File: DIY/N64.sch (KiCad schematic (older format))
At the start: 5 parts, among them P1 N64 Ctrl slot, P2 N64 Ctrl slot, P3 N64 Ctrl slot, P4 N64 Ctrl slot

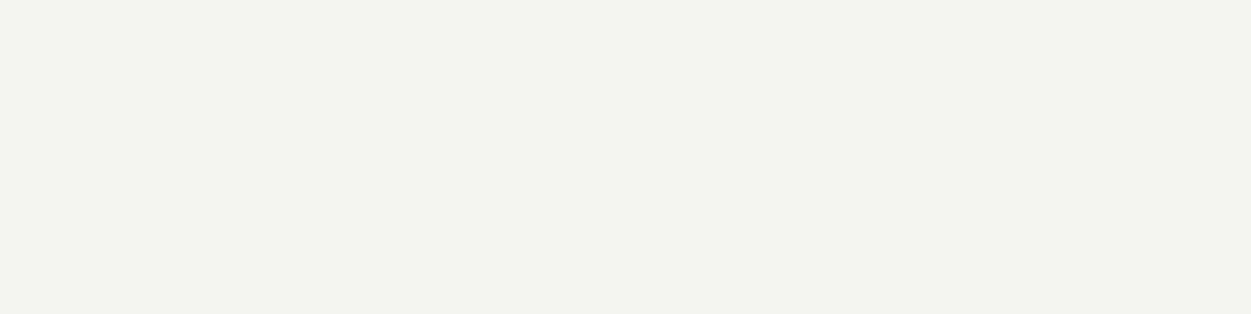
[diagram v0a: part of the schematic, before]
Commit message: [DIY] Add note to cable schematics to underline how important I39 is.
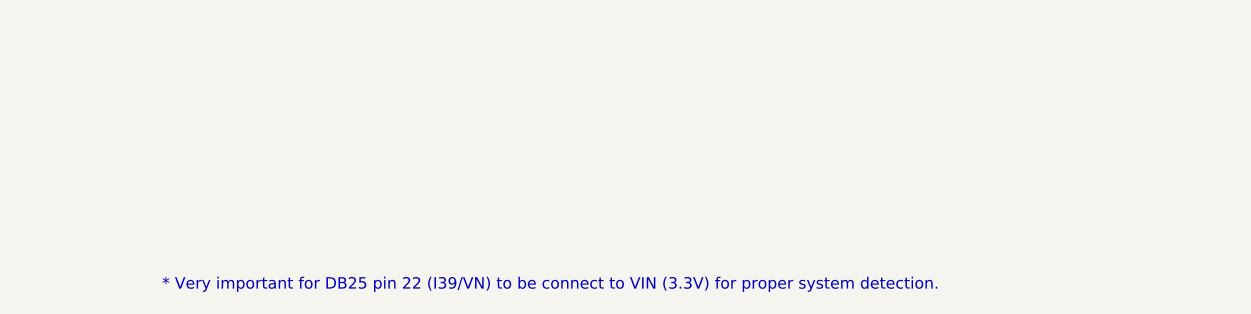
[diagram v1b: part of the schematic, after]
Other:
- note added: "* Very important for DB25 pin 22 (I39/VN) to be connect to VIN (3.3V) for proper system detection."
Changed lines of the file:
@@
 	6100 4650 6100 4550
 Connection ~ 6100 4550
+Text Notes 6350 6900 0    50   ~ 0
+* Very important for DB25 pin 22 (I39/VN) to be connect to VIN (3.3V) for proper system detection.
 $EndSCHEMATC

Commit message: Use new port symbol in cable schematic
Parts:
- P1, P2, P3, P4: symbol Connector_Generic:Conn_01x03 -> Connector_Gaming:N64
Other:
- note added: "Connectors facing console"
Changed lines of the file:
@@
 Sheet 5 7
 Title "BlueRetro - N64 adapter cable"
-Date "2020-08-22"
-Rev "v1.1"
-Comp ""
+Date "2020-10-02"
+Rev "v1.2"
+Comp "©2020 Jacques Gagnon, licensed under CC-BY-4.0"
 Comment1 ""
 Comment2 ""
@@
 $EndDescr
 $Comp
-L Connector_Generic:Conn_01x03 P?
+L Connector_Gaming:N64 P?
 U 1 1 5F47F7C8
-P 4650 2600
+P 4550 2500
 AR Path="/5F47F7C8" Ref="P?"  Part="1"
 AR Path="/5F457716/5F47F7C8" Ref="P1"  Part="1"
-F 0 "P1" H 4568 2917 50  0000 C CNN
-F 1 "N64 Ctrl slot" H 4568 2826 50  0000 C CNN
-F 2 "" H 4650 2600 50  0001 C CNN
-F 3 "~" H 4650 2600 50  0001 C CNN
-	1    4650 2600
-	-1   0    0    -1
-$EndComp
-$Comp
-L Connector_Generic:Conn_01x03 P?
+F 0 "P1" H 4550 2250 50  0000 C CNN
+F 1 "N64 Ctrl slot" H 4550 2350 50  0000 C CNN
+F 2 "" H 4550 2500 50  0001 C CNN
+F 3 "~" H 4550 2500 50  0001 C CNN
+	1    4550 2500
+	-1   0    0    1
+$EndComp
+$Comp
+L Connector_Gaming:N64 P?
 U 1 1 5F47F7CE
-P 4650 3250
+P 4550 3150
 AR Path="/5F47F7CE" Ref="P?"  Part="1"
 AR Path="/5F457716/5F47F7CE" Ref="P2"  Part="1"
-F 0 "P2" H 4568 3567 50  0000 C CNN
-F 1 "N64 Ctrl slot" H 4568 3476 50  0000 C CNN
-F 2 "" H 4650 3250 50  0001 C CNN
-F 3 "~" H 4650 3250 50  0001 C CNN
-	1    4650 3250
-	-1   0    0    -1
-$EndComp
-$Comp
-L Connector_Generic:Conn_01x03 P?
+F 0 "P2" H 4550 2900 50  0000 C CNN
+F 1 "N64 Ctrl slot" H 4550 3000 50  0000 C CNN
+F 2 "" H 4550 3150 50  0001 C CNN
+F 3 "~" H 4550 3150 50  0001 C CNN
+	1    4550 3150
+	-1   0    0    1
+$EndComp
+$Comp
+L Connector_Gaming:N64 P?
 U 1 1 5F47F7D4
-P 4650 3900
+P 4550 3800
 AR Path="/5F47F7D4" Ref="P?"  Part="1"
 AR Path="/5F457716/5F47F7D4" Ref="P3"  Part="1"
-F 0 "P3" H 4568 4217 50  0000 C CNN
-F 1 "N64 Ctrl slot" H 4568 4126 50  0000 C CNN
-F 2 "" H 4650 3900 50  0001 C CNN
-F 3 "~" H 4650 3900 50  0001 C CNN
-	1    4650 3900
-	-1   0    0    -1
-$EndComp
-$Comp
-L Connector_Generic:Conn_01x03 P?
+F 0 "P3" H 4550 3550 50  0000 C CNN
+F 1 "N64 Ctrl slot" H 4550 3650 50  0000 C CNN
+F 2 "" H 4550 3800 50  0001 C CNN
+F 3 "~" H 4550 3800 50  0001 C CNN
+	1    4550 3800
+	-1   0    0    1
+$EndComp
+$Comp
+L Connector_Gaming:N64 P?
 U 1 1 5F47F7DA
-P 4650 4550
+P 4550 4450
 AR Path="/5F47F7DA" Ref="P?"  Part="1"
 AR Path="/5F457716/5F47F7DA" Ref="P4"  Part="1"
-F 0 "P4" H 4568 4867 50  0000 C CNN
-F 1 "N64 Ctrl slot" H 4568 4776 50  0000 C CNN
-F 2 "" H 4650 4550 50  0001 C CNN
-F 3 "~" H 4650 4550 50  0001 C CNN
-	1    4650 4550
-	-1   0    0    -1
+F 0 "P4" H 4550 4200 50  0000 C CNN
+F 1 "N64 Ctrl slot" H 4550 4300 50  0000 C CNN
+F 2 "" H 4550 4450 50  0001 C CNN
+F 3 "~" H 4550 4450 50  0001 C CNN
+	1    4550 4450
+	-1   0    0    1
 $EndComp
 $Comp
@@
 Text Notes 6350 6900 0    50   ~ 0
 * Very important for DB25 pin 22 (I39/VN) to be connect to VIN (3.3V) for proper system detection.
+Text Notes 3250 3500 0    50   ~ 0
+Connectors facing console
 $EndSCHEMATC

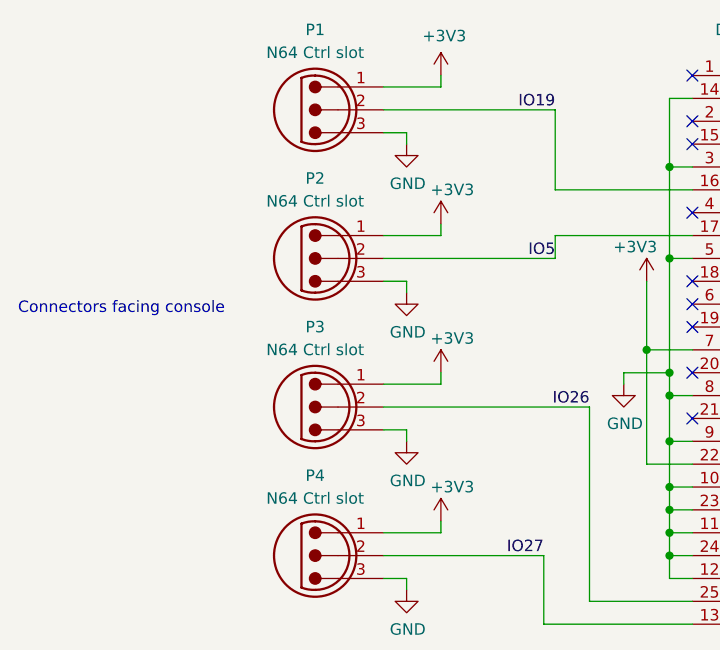
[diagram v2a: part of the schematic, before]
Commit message: Update adapter cable schematics
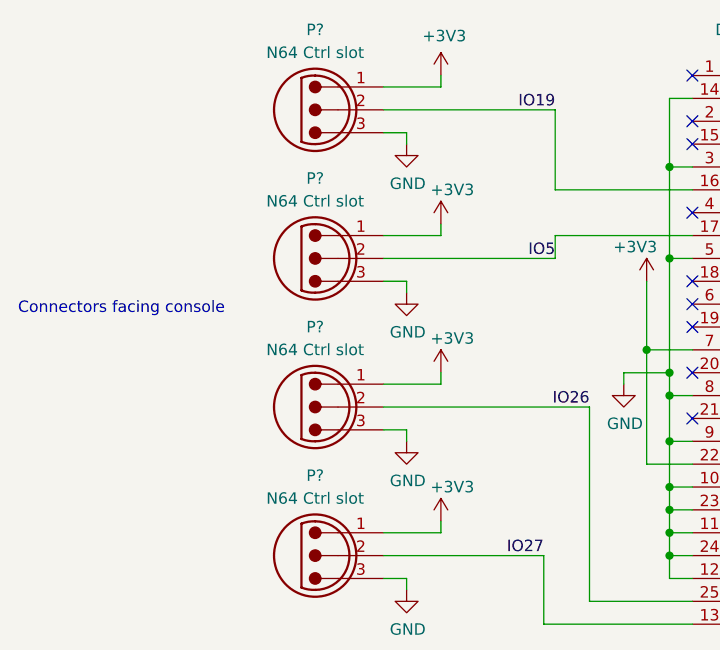
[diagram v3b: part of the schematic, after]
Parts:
- gave numbers to parts that had none: 1
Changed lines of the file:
@@
 $Descr USLetter 11000 8500
 encoding utf-8
-Sheet 5 7
+Sheet 5 10
 Title "BlueRetro - N64 adapter cable"
 Date "2020-10-02"
@@
 AR Path="/5F47F7C8" Ref="P?"  Part="1"
 AR Path="/5F457716/5F47F7C8" Ref="P1"  Part="1"
-F 0 "P1" H 4550 2250 50  0000 C CNN
+F 0 "P?" H 4550 2250 50  0000 C CNN
 F 1 "N64 Ctrl slot" H 4550 2350 50  0000 C CNN
 F 2 "" H 4550 2500 50  0001 C CNN
@@
 AR Path="/5F47F7CE" Ref="P?"  Part="1"
 AR Path="/5F457716/5F47F7CE" Ref="P2"  Part="1"
-F 0 "P2" H 4550 2900 50  0000 C CNN
+F 0 "P?" H 4550 2900 50  0000 C CNN
 F 1 "N64 Ctrl slot" H 4550 3000 50  0000 C CNN
 F 2 "" H 4550 3150 50  0001 C CNN
@@
 AR Path="/5F47F7D4" Ref="P?"  Part="1"
 AR Path="/5F457716/5F47F7D4" Ref="P3"  Part="1"
-F 0 "P3" H 4550 3550 50  0000 C CNN
+F 0 "P?" H 4550 3550 50  0000 C CNN
 F 1 "N64 Ctrl slot" H 4550 3650 50  0000 C CNN
 F 2 "" H 4550 3800 50  0001 C CNN
@@
 AR Path="/5F47F7DA" Ref="P?"  Part="1"
 AR Path="/5F457716/5F47F7DA" Ref="P4"  Part="1"
-F 0 "P4" H 4550 4200 50  0000 C CNN
+F 0 "P?" H 4550 4200 50  0000 C CNN
 F 1 "N64 Ctrl slot" H 4550 4300 50  0000 C CNN
 F 2 "" H 4550 4450 50  0001 C CNN
@@
 P 4950 4050
 AR Path="/5F47F7E0" Ref="#PWR?"  Part="1"
-AR Path="/5F457716/5F47F7E0" Ref="#PWR?"  Part="1"
+AR Path="/5F457716/5F47F7E0" Ref="#PWR094"  Part="1"
 F 0 "#PWR?" H 4950 3800 50  0001 C CNN
 F 1 "GND" H 4955 3877 50  0000 C CNN
@@
 P 5100 2450
 AR Path="/5F47F7E6" Ref="#PWR?"  Part="1"
-AR Path="/5F457716/5F47F7E6" Ref="#PWR?"  Part="1"
+AR Path="/5F457716/5F47F7E6" Ref="#PWR096"  Part="1"
 F 0 "#PWR?" H 5100 2300 50  0001 C CNN
 F 1 "+3V3" H 5115 2623 50  0000 C CNN
@@
 P 5100 3100
 AR Path="/5F47F7EC" Ref="#PWR?"  Part="1"
-AR Path="/5F457716/5F47F7EC" Ref="#PWR?"  Part="1"
+AR Path="/5F457716/5F47F7EC" Ref="#PWR097"  Part="1"
 F 0 "#PWR?" H 5100 2950 50  0001 C CNN
 F 1 "+3V3" H 5150 3250 50  0000 C CNN
@@
 P 5100 3750
 AR Path="/5F47F7F2" Ref="#PWR?"  Part="1"
-AR Path="/5F457716/5F47F7F2" Ref="#PWR?"  Part="1"
+AR Path="/5F457716/5F47F7F2" Ref="#PWR098"  Part="1"
 F 0 "#PWR?" H 5100 3600 50  0001 C CNN
 F 1 "+3V3" H 5150 3900 50  0000 C CNN
@@
 P 5100 4400
 AR Path="/5F47F7F8" Ref="#PWR?"  Part="1"
-AR Path="/5F457716/5F47F7F8" Ref="#PWR?"  Part="1"
+AR Path="/5F457716/5F47F7F8" Ref="#PWR099"  Part="1"
 F 0 "#PWR?" H 5100 4250 50  0001 C CNN
 F 1 "+3V3" H 5150 4550 50  0000 C CNN
@@
 P 4950 4700
 AR Path="/5F47F7FE" Ref="#PWR?"  Part="1"
-AR Path="/5F457716/5F47F7FE" Ref="#PWR?"  Part="1"
+AR Path="/5F457716/5F47F7FE" Ref="#PWR095"  Part="1"
 F 0 "#PWR?" H 4950 4450 50  0001 C CNN
 F 1 "GND" H 4955 4527 50  0000 C CNN
@@
 P 4950 3400
 AR Path="/5F47F804" Ref="#PWR?"  Part="1"
-AR Path="/5F457716/5F47F804" Ref="#PWR?"  Part="1"
+AR Path="/5F457716/5F47F804" Ref="#PWR093"  Part="1"
 F 0 "#PWR?" H 4950 3150 50  0001 C CNN
 F 1 "GND" H 4955 3227 50  0000 C CNN
@@
 P 4950 2750
 AR Path="/5F47F80A" Ref="#PWR?"  Part="1"
-AR Path="/5F457716/5F47F80A" Ref="#PWR?"  Part="1"
+AR Path="/5F457716/5F47F80A" Ref="#PWR092"  Part="1"
 F 0 "#PWR?" H 4950 2500 50  0001 C CNN
 F 1 "GND" H 4955 2577 50  0000 C CNN
@@
 P 6000 3350
 AR Path="/5F47F822" Ref="#PWR?"  Part="1"
-AR Path="/5F457716/5F47F822" Ref="#PWR?"  Part="1"
+AR Path="/5F457716/5F47F822" Ref="#PWR0101"  Part="1"
 F 0 "#PWR?" H 6000 3200 50  0001 C CNN
 F 1 "+3V3" H 5950 3500 50  0000 C CNN
@@
 P 5900 3800
 AR Path="/5F47F828" Ref="#PWR?"  Part="1"
-AR Path="/5F457716/5F47F828" Ref="#PWR?"  Part="1"
+AR Path="/5F457716/5F47F828" Ref="#PWR0100"  Part="1"
 F 0 "#PWR?" H 5900 3550 50  0001 C CNN
 F 1 "GND" H 5905 3627 50  0000 C CNN
@@
 P 6500 3650
 AR Path="/5F47F7C2" Ref="J?"  Part="1"
-AR Path="/5F457716/5F47F7C2" Ref="J?"  Part="1"
+AR Path="/5F457716/5F47F7C2" Ref="J7"  Part="1"
 F 0 "J?" H 6680 3696 50  0001 L CNN
 F 1 "DB25_Male" H 6300 2250 50  0000 L CNN
